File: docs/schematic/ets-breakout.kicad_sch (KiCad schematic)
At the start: 26 parts, among them J5 QSE-040-01-L-D-A, K0 MCX-J-P-H-ST-SM1, K1 MCX-J-P-H-ST-SM1, K10 MCX-J-P-H-ST-SM1, K11 MCX-J-P-H-ST-SM1, K12 MCX-J-P-H-ST-SM1, K13 MCX-J-P-H-ST-SM1, K14 MCX-J-P-H-ST-SM1, K15 MCX-J-P-H-ST-SM1, K16 MCX-J-P-H-ST-SM1, K17 MCX-J-P-H-ST-SM1, K18 MCX-J-P-H-ST-SM1, K19 MCX-J-P-H-ST-SM1, K2 MCX-J-P-H-ST-SM1, K20 MCX-J-P-H-ST-SM1, K21 MCX-J-P-H-ST-SM1, K22 MCX-J-P-H-ST-SM1, K23 MCX-J-P-H-ST-SM1, K3 MCX-J-P-H-ST-SM1, K4 MCX-J-P-H-ST-SM1, K5 MCX-J-P-H-ST-SM1, K6 MCX-J-P-H-ST-SM1, K7 MCX-J-P-H-ST-SM1, K8 MCX-J-P-H-ST-SM1, K9 MCX-J-P-H-ST-SM1

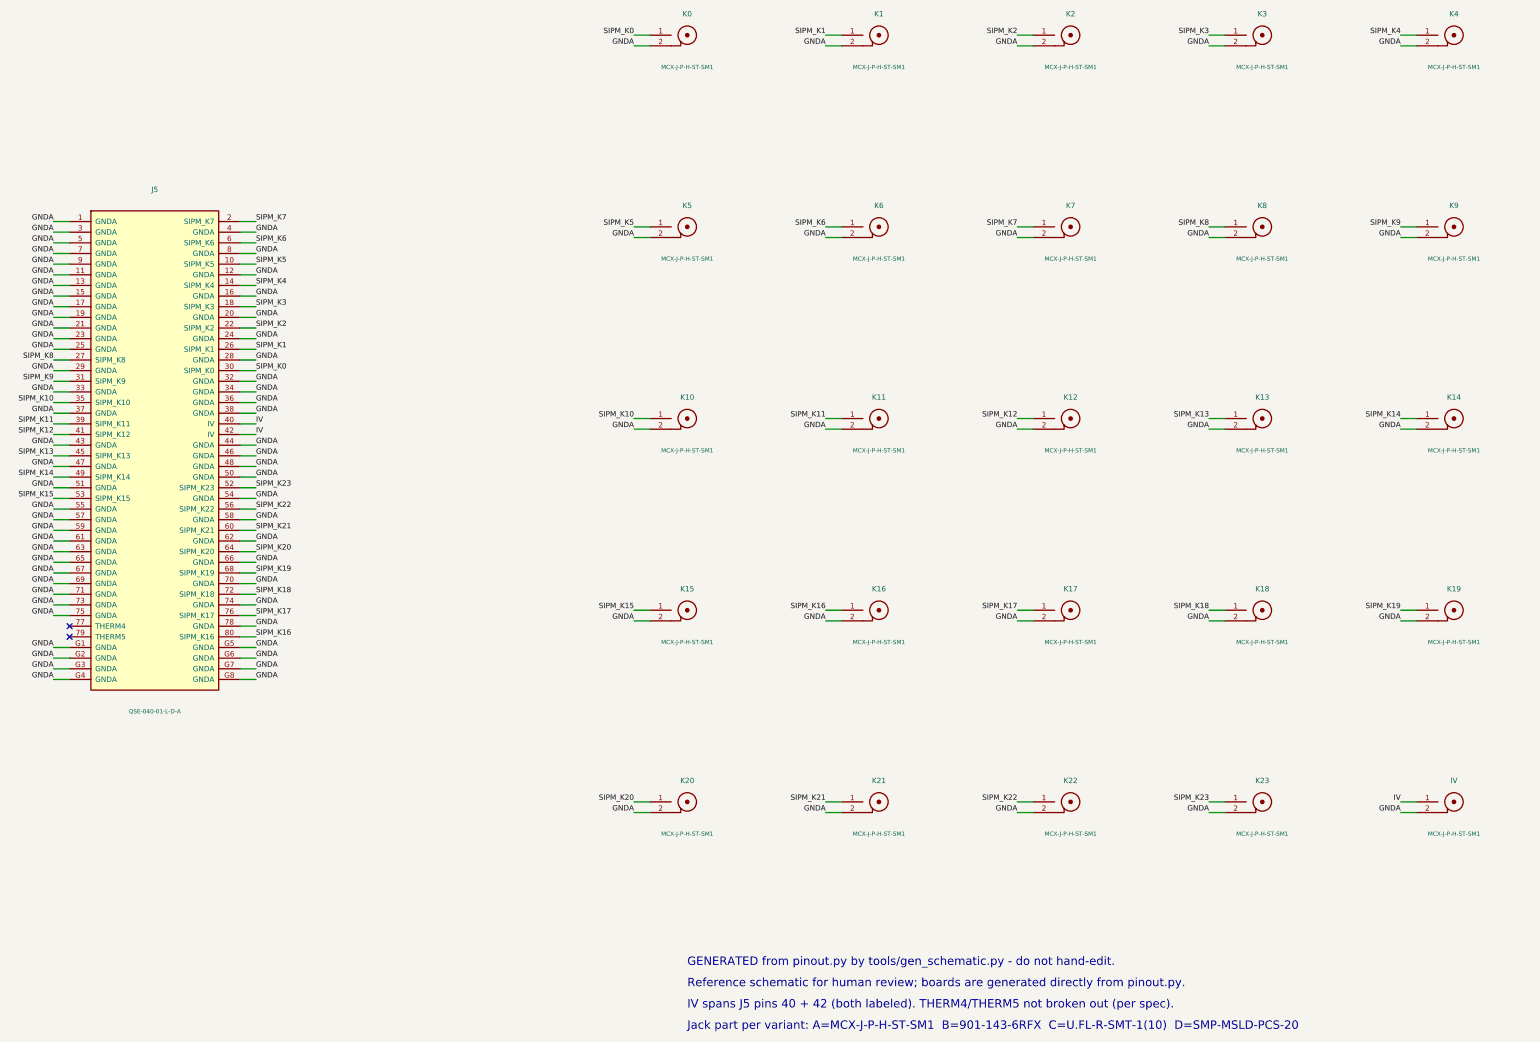
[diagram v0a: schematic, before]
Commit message: Board A: through-hole MCX + 8/16 planar FreeRouting autoroute (JLC)
Re-lay-out Board A to eliminate the connector-crossing tracks and the
per-jack signal vias the reviewer flagged:

- Jack SMD -> THROUGH-HOLE: Samtec MCX-J-P-H-ST-TH1 (DK SAM8944-ND). The
  plated signal pin reaches every layer, so the QSE B.Cu escape lands on
  it with no face-change via. New datasheet-verified footprint + drawing.
- Placement 12/12 -> 8/16 planar: each jack sits on the edge matching its
  QSE pin column (west 8 = K8-K15, east 16 + IV), a monotonic single-layer
  fan. The old 12/12 forced 4 channels across the connector (the crossings);
  12/12 kept as gen_board SPLIT="balanced" flag.
- Routing now via FreeRouting (KiCad -> .dsn -> autoroute -> .ses), B.Cu
  only: ZERO signal vias, ZERO crossings, all 25 nets on one layer. New
  tools export_dsn.py / import_ses.py / tie_islands.py; finalize_board.py
  gains setup/stitch modes (B/C/D keep the deterministic router).
- Fab JLCPCB-only: 0.325 mm 50 ohm microstrip on JLC04161H-7628 (was 0.34
  on the PCBWay stack); order controlled impedance. Board now 75 x 157 mm.
- DRC 0 violations / 0 unconnected; netlist verified identical to pinout.py.
- Fab package, JLC upload zip, DigiKey BOM, all docs + reference schematic
  regenerated. Purchase total ~$950 (MCX 120 @ $4.21 + QSE 5 + IV adapter 4).

Adversarially verified: board (0 signal vias, single-layer, DRC), fab
package, and cross-doc consistency.

Co-Authored-By: Claude Fable 5 <noreply@anthropic.com>
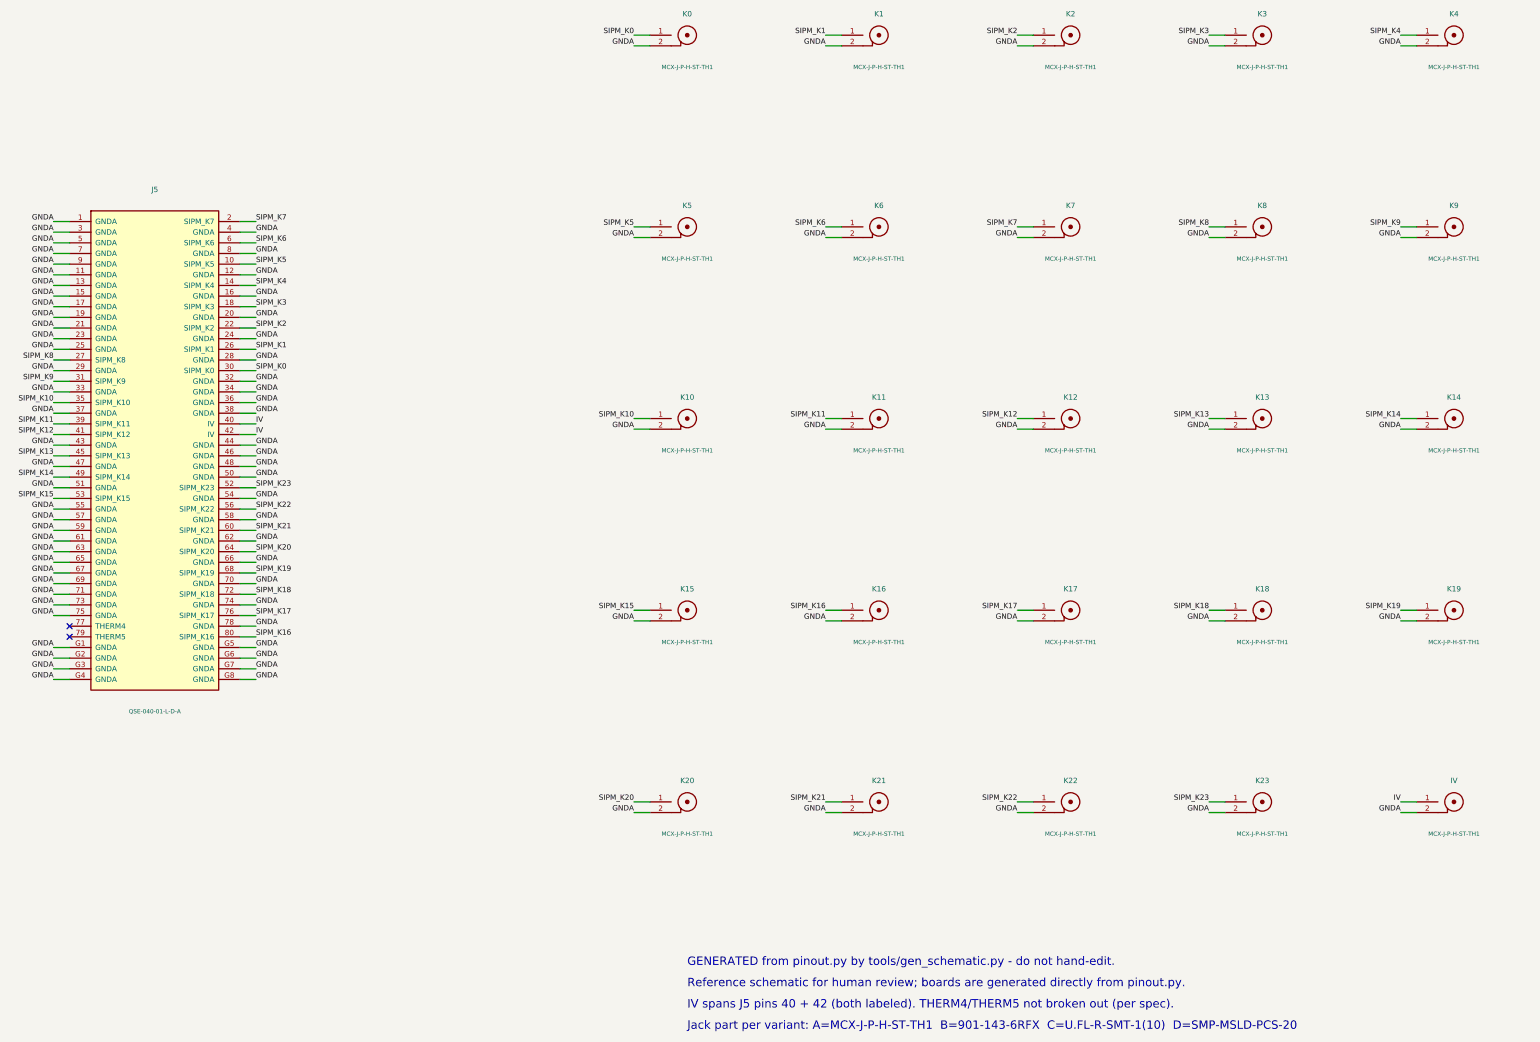
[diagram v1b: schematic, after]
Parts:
- IV, K0, K1, K10, K11, K12, K13, K14, K15, K16, K17, K18, K19, K2, K20, K21, K22, K23, K3, K4, K5, K6, K7, K8, K9: value MCX-J-P-H-ST-SM1 -> MCX-J-P-H-ST-TH1
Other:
- note added: "Jack part per variant: A=MCX-J-P-H-ST-TH1 B=901-143-6RFX C=U.FL-R-SMT-1(10) D=SMP-MSLD-PCS-20"
- note removed: "Jack part per variant: A=MCX-J-P-H-ST-SM1 B=901-143-6RFX C=U.FL-R-SMT-1(10) D=SMP-MSLD-PCS-20"
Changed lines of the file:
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@@
 		(dnp no)
 		(property "Reference" "K0" (at 190.5 44.449999999999996 0) (effects (font (size 1.27 1.27))))
-		(property "Value" "MCX-J-P-H-ST-SM1" (at 190.5 57.15 0) (effects (font (size 1.0 1.0))))
+		(property "Value" "MCX-J-P-H-ST-TH1" (at 190.5 57.15 0) (effects (font (size 1.0 1.0))))
 		(instances
 			(project "ets-breakout"
@@
 		(dnp no)
 		(property "Reference" "K1" (at 236.22 44.449999999999996 0) (effects (font (size 1.27 1.27))))
-		(property "Value" "MCX-J-P-H-ST-SM1" (at 236.22 57.15 0) (effects (font (size 1.0 1.0))))
+		(property "Value" "MCX-J-P-H-ST-TH1" (at 236.22 57.15 0) (effects (font (size 1.0 1.0))))
 		(instances
 			(project "ets-breakout"
@@
 		(dnp no)
 		(property "Reference" "K2" (at 281.94 44.449999999999996 0) (effects (font (size 1.27 1.27))))
-		(property "Value" "MCX-J-P-H-ST-SM1" (at 281.94 57.15 0) (effects (font (size 1.0 1.0))))
+		(property "Value" "MCX-J-P-H-ST-TH1" (at 281.94 57.15 0) (effects (font (size 1.0 1.0))))
 		(instances
 			(project "ets-breakout"
@@
 		(dnp no)
 		(property "Reference" "K3" (at 327.66 44.449999999999996 0) (effects (font (size 1.27 1.27))))
-		(property "Value" "MCX-J-P-H-ST-SM1" (at 327.66 57.15 0) (effects (font (size 1.0 1.0))))
+		(property "Value" "MCX-J-P-H-ST-TH1" (at 327.66 57.15 0) (effects (font (size 1.0 1.0))))
 		(instances
 			(project "ets-breakout"
@@
 		(dnp no)
 		(property "Reference" "K4" (at 373.38 44.449999999999996 0) (effects (font (size 1.27 1.27))))
-		(property "Value" "MCX-J-P-H-ST-SM1" (at 373.38 57.15 0) (effects (font (size 1.0 1.0))))
+		(property "Value" "MCX-J-P-H-ST-TH1" (at 373.38 57.15 0) (effects (font (size 1.0 1.0))))
 		(instances
 			(project "ets-breakout"
@@
 		(dnp no)
 		(property "Reference" "K5" (at 190.5 90.17 0) (effects (font (size 1.27 1.27))))
-		(property "Value" "MCX-J-P-H-ST-SM1" (at 190.5 102.86999999999999 0) (effects (font (size 1.0 1.0))))
+		(property "Value" "MCX-J-P-H-ST-TH1" (at 190.5 102.86999999999999 0) (effects (font (size 1.0 1.0))))
 		(instances
 			(project "ets-breakout"
@@
 		(dnp no)
 		(property "Reference" "K6" (at 236.22 90.17 0) (effects (font (size 1.27 1.27))))
-		(property "Value" "MCX-J-P-H-ST-SM1" (at 236.22 102.86999999999999 0) (effects (font (size 1.0 1.0))))
+		(property "Value" "MCX-J-P-H-ST-TH1" (at 236.22 102.86999999999999 0) (effects (font (size 1.0 1.0))))
 		(instances
 			(project "ets-breakout"
@@
 		(dnp no)
 		(property "Reference" "K7" (at 281.94 90.17 0) (effects (font (size 1.27 1.27))))
-		(property "Value" "MCX-J-P-H-ST-SM1" (at 281.94 102.86999999999999 0) (effects (font (size 1.0 1.0))))
+		(property "Value" "MCX-J-P-H-ST-TH1" (at 281.94 102.86999999999999 0) (effects (font (size 1.0 1.0))))
 		(instances
 			(project "ets-breakout"
@@
 		(dnp no)
 		(property "Reference" "K8" (at 327.66 90.17 0) (effects (font (size 1.27 1.27))))
-		(property "Value" "MCX-J-P-H-ST-SM1" (at 327.66 102.86999999999999 0) (effects (font (size 1.0 1.0))))
+		(property "Value" "MCX-J-P-H-ST-TH1" (at 327.66 102.86999999999999 0) (effects (font (size 1.0 1.0))))
 		(instances
 			(project "ets-breakout"
@@
 		(dnp no)
 		(property "Reference" "K9" (at 373.38 90.17 0) (effects (font (size 1.27 1.27))))
-		(property "Value" "MCX-J-P-H-ST-SM1" (at 373.38 102.86999999999999 0) (effects (font (size 1.0 1.0))))
+		(property "Value" "MCX-J-P-H-ST-TH1" (at 373.38 102.86999999999999 0) (effects (font (size 1.0 1.0))))
 		(instances
 			(project "ets-breakout"
@@
 		(dnp no)
 		(property "Reference" "K10" (at 190.5 135.89000000000001 0) (effects (font (size 1.27 1.27))))
-		(property "Value" "MCX-J-P-H-ST-SM1" (at 190.5 148.59 0) (effects (font (size 1.0 1.0))))
+		(property "Value" "MCX-J-P-H-ST-TH1" (at 190.5 148.59 0) (effects (font (size 1.0 1.0))))
 		(instances
 			(project "ets-breakout"
@@
 		(dnp no)
 		(property "Reference" "K11" (at 236.22 135.89000000000001 0) (effects (font (size 1.27 1.27))))
-		(property "Value" "MCX-J-P-H-ST-SM1" (at 236.22 148.59 0) (effects (font (size 1.0 1.0))))
+		(property "Value" "MCX-J-P-H-ST-TH1" (at 236.22 148.59 0) (effects (font (size 1.0 1.0))))
 		(instances
 			(project "ets-breakout"
@@
 		(dnp no)
 		(property "Reference" "K12" (at 281.94 135.89000000000001 0) (effects (font (size 1.27 1.27))))
-		(property "Value" "MCX-J-P-H-ST-SM1" (at 281.94 148.59 0) (effects (font (size 1.0 1.0))))
+		(property "Value" "MCX-J-P-H-ST-TH1" (at 281.94 148.59 0) (effects (font (size 1.0 1.0))))
 		(instances
 			(project "ets-breakout"
@@
 		(dnp no)
 		(property "Reference" "K13" (at 327.66 135.89000000000001 0) (effects (font (size 1.27 1.27))))
-		(property "Value" "MCX-J-P-H-ST-SM1" (at 327.66 148.59 0) (effects (font (size 1.0 1.0))))
+		(property "Value" "MCX-J-P-H-ST-TH1" (at 327.66 148.59 0) (effects (font (size 1.0 1.0))))
 		(instances
 			(project "ets-breakout"
@@
 		(dnp no)
 		(property "Reference" "K14" (at 373.38 135.89000000000001 0) (effects (font (size 1.27 1.27))))
-		(property "Value" "MCX-J-P-H-ST-SM1" (at 373.38 148.59 0) (effects (font (size 1.0 1.0))))
+		(property "Value" "MCX-J-P-H-ST-TH1" (at 373.38 148.59 0) (effects (font (size 1.0 1.0))))
 		(instances
 			(project "ets-breakout"
@@
 		(dnp no)
 		(property "Reference" "K15" (at 190.5 181.61 0) (effects (font (size 1.27 1.27))))
-		(property "Value" "MCX-J-P-H-ST-SM1" (at 190.5 194.31 0) (effects (font (size 1.0 1.0))))
+		(property "Value" "MCX-J-P-H-ST-TH1" (at 190.5 194.31 0) (effects (font (size 1.0 1.0))))
 		(instances
 			(project "ets-breakout"
@@
 		(dnp no)
 		(property "Reference" "K16" (at 236.22 181.61 0) (effects (font (size 1.27 1.27))))
-		(property "Value" "MCX-J-P-H-ST-SM1" (at 236.22 194.31 0) (effects (font (size 1.0 1.0))))
+		(property "Value" "MCX-J-P-H-ST-TH1" (at 236.22 194.31 0) (effects (font (size 1.0 1.0))))
 		(instances
 			(project "ets-breakout"
@@
 		(dnp no)
 		(property "Reference" "K17" (at 281.94 181.61 0) (effects (font (size 1.27 1.27))))
-		(property "Value" "MCX-J-P-H-ST-SM1" (at 281.94 194.31 0) (effects (font (size 1.0 1.0))))
+		(property "Value" "MCX-J-P-H-ST-TH1" (at 281.94 194.31 0) (effects (font (size 1.0 1.0))))
 		(instances
 			(project "ets-breakout"
@@
 		(dnp no)
 		(property "Reference" "K18" (at 327.66 181.61 0) (effects (font (size 1.27 1.27))))
-		(property "Value" "MCX-J-P-H-ST-SM1" (at 327.66 194.31 0) (effects (font (size 1.0 1.0))))
+		(property "Value" "MCX-J-P-H-ST-TH1" (at 327.66 194.31 0) (effects (font (size 1.0 1.0))))
 		(instances
 			(project "ets-breakout"
@@
 		(dnp no)
 		(property "Reference" "K19" (at 373.38 181.61 0) (effects (font (size 1.27 1.27))))
-		(property "Value" "MCX-J-P-H-ST-SM1" (at 373.38 194.31 0) (effects (font (size 1.0 1.0))))
+		(property "Value" "MCX-J-P-H-ST-TH1" (at 373.38 194.31 0) (effects (font (size 1.0 1.0))))
 		(instances
 			(project "ets-breakout"
@@
 		(dnp no)
 		(property "Reference" "K20" (at 190.5 227.33 0) (effects (font (size 1.27 1.27))))
-		(property "Value" "MCX-J-P-H-ST-SM1" (at 190.5 240.03 0) (effects (font (size 1.0 1.0))))
+		(property "Value" "MCX-J-P-H-ST-TH1" (at 190.5 240.03 0) (effects (font (size 1.0 1.0))))
 		(instances
 			(project "ets-breakout"
@@
 		(dnp no)
 		(property "Reference" "K21" (at 236.22 227.33 0) (effects (font (size 1.27 1.27))))
-		(property "Value" "MCX-J-P-H-ST-SM1" (at 236.22 240.03 0) (effects (font (size 1.0 1.0))))
+		(property "Value" "MCX-J-P-H-ST-TH1" (at 236.22 240.03 0) (effects (font (size 1.0 1.0))))
 		(instances
 			(project "ets-breakout"
@@
 		(dnp no)
 		(property "Reference" "K22" (at 281.94 227.33 0) (effects (font (size 1.27 1.27))))
-		(property "Value" "MCX-J-P-H-ST-SM1" (at 281.94 240.03 0) (effects (font (size 1.0 1.0))))
+		(property "Value" "MCX-J-P-H-ST-TH1" (at 281.94 240.03 0) (effects (font (size 1.0 1.0))))
 		(instances
 			(project "ets-breakout"
@@
 		(dnp no)
 		(property "Reference" "K23" (at 327.66 227.33 0) (effects (font (size 1.27 1.27))))
-		(property "Value" "MCX-J-P-H-ST-SM1" (at 327.66 240.03 0) (effects (font (size 1.0 1.0))))
+		(property "Value" "MCX-J-P-H-ST-TH1" (at 327.66 240.03 0) (effects (font (size 1.0 1.0))))
 		(instances
 			(project "ets-breakout"
@@
 		(dnp no)
 		(property "Reference" "IV" (at 373.38 227.33 0) (effects (font (size 1.27 1.27))))
-		(property "Value" "MCX-J-P-H-ST-SM1" (at 373.38 240.03 0) (effects (font (size 1.0 1.0))))
+		(property "Value" "MCX-J-P-H-ST-TH1" (at 373.38 240.03 0) (effects (font (size 1.0 1.0))))
 		(instances
 			(project "ets-breakout"
@@
 		(effects (font (size 2.0 2.0)) (justify left bottom))
 	)
-	(text "Jack part per variant: A=MCX-J-P-H-ST-SM1  B=901-143-6RFX  C=U.FL-R-SMT-1(10)  D=SMP-MSLD-PCS-20"
+	(text "Jack part per variant: A=MCX-J-P-H-ST-TH1  B=901-143-6RFX  C=U.FL-R-SMT-1(10)  D=SMP-MSLD-PCS-20"
 		(exclude_from_sim no)
 		(at 190.5 287.02 0)
